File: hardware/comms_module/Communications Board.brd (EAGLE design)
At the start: 33.5 x 32.1 mm, 68 parts, among them U1 Value, U2 STC3115, X2 USB-MICROB, Y1 32.768kHz, Y2 24MHz

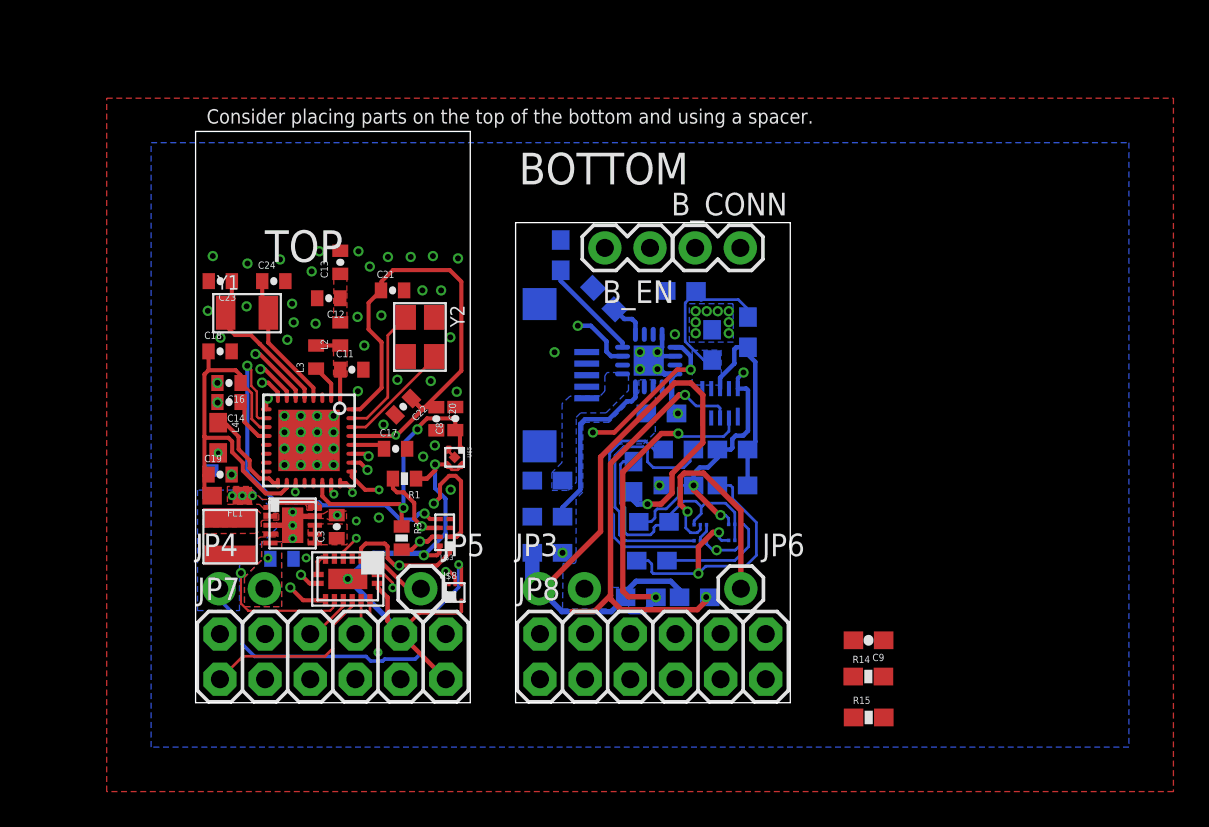
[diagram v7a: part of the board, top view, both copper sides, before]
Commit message: App PCB Trace Antenna
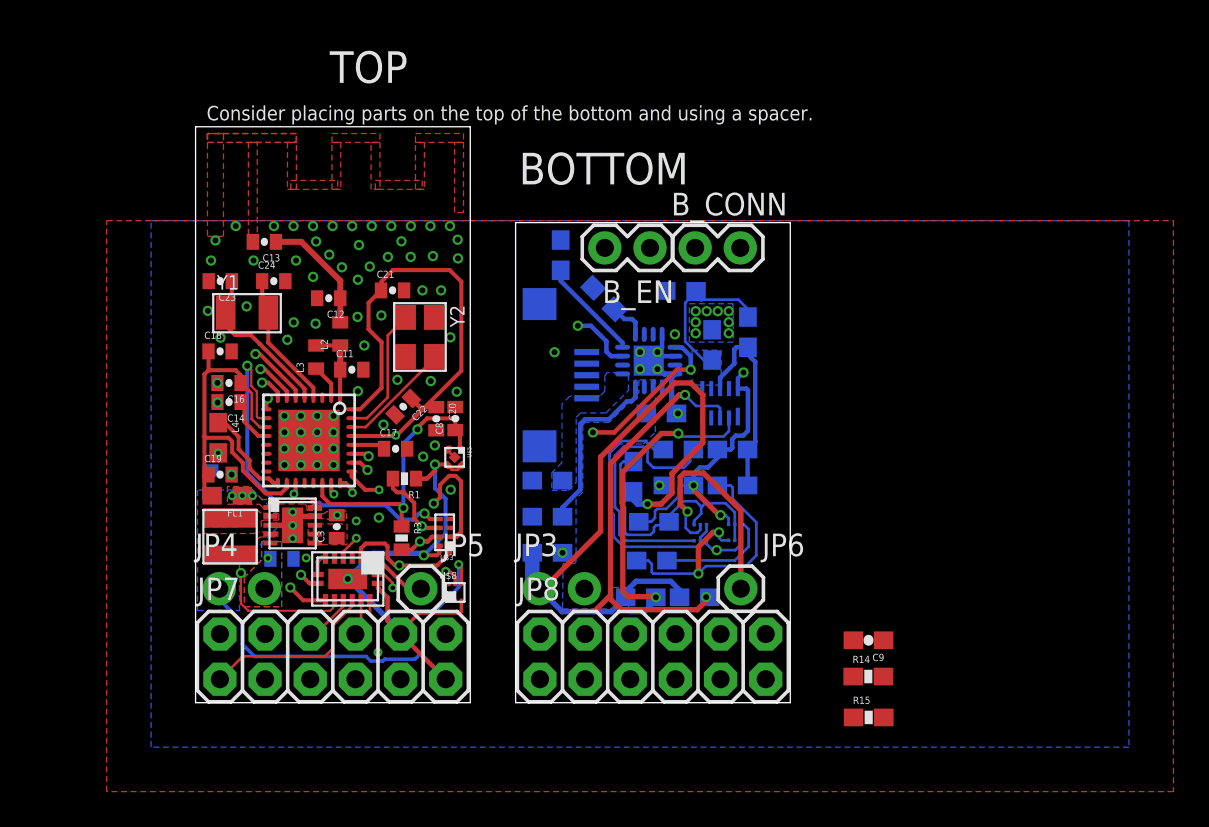
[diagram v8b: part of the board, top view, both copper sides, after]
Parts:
- moved C13 4.42 mm to (3.87, 25.9), turned to 180 degrees
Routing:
- net N$41: track 0.00 -> 6.87 mm
- net MPSW: track 21.8 -> 19.4 mm
- net +3V3: track 61.7 -> 59.5 mm
- net RF_P: track 2.94 -> 4.30 mm
- net GND: vias 76 -> 92
- added copper zone on layer 1, net ANTENNA
- removed copper zone on layer 1, net N$41
- removed copper zone on layer 1, net RF_P
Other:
- board size 33.5 x 32.1 mm -> 33.5 x 32.4 mm
